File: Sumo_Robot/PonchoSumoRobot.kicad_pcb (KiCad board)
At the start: 2 copper layers, 85.9 x 137.2 mm, 58 parts, among them K1 RELAY_C, K2 RELAY_C, K3 RELAY_C, K4 RELAY_C, P1 CONN_01X02, P11 CONN_01X02, P12 CONN_01X02, P13 CONN_01X02, P14 CONN_01X02, P15 CONN_01X02, P16 CONN_01X02, P17 CONN_01X02, P18 CONN_01X02, P2 CONN_01X04, P3 CONN_02X09, P4 CONN_01X02, P5 CONN_01X02, P6 CONN_01X04, P7 CONN_01X02, P8 CONN_01X02, Q1 2SC1945, Q2 2SC1945, Q3 2SC1945, Q4 2SC1945, Q5 2SC1945, U5 40106

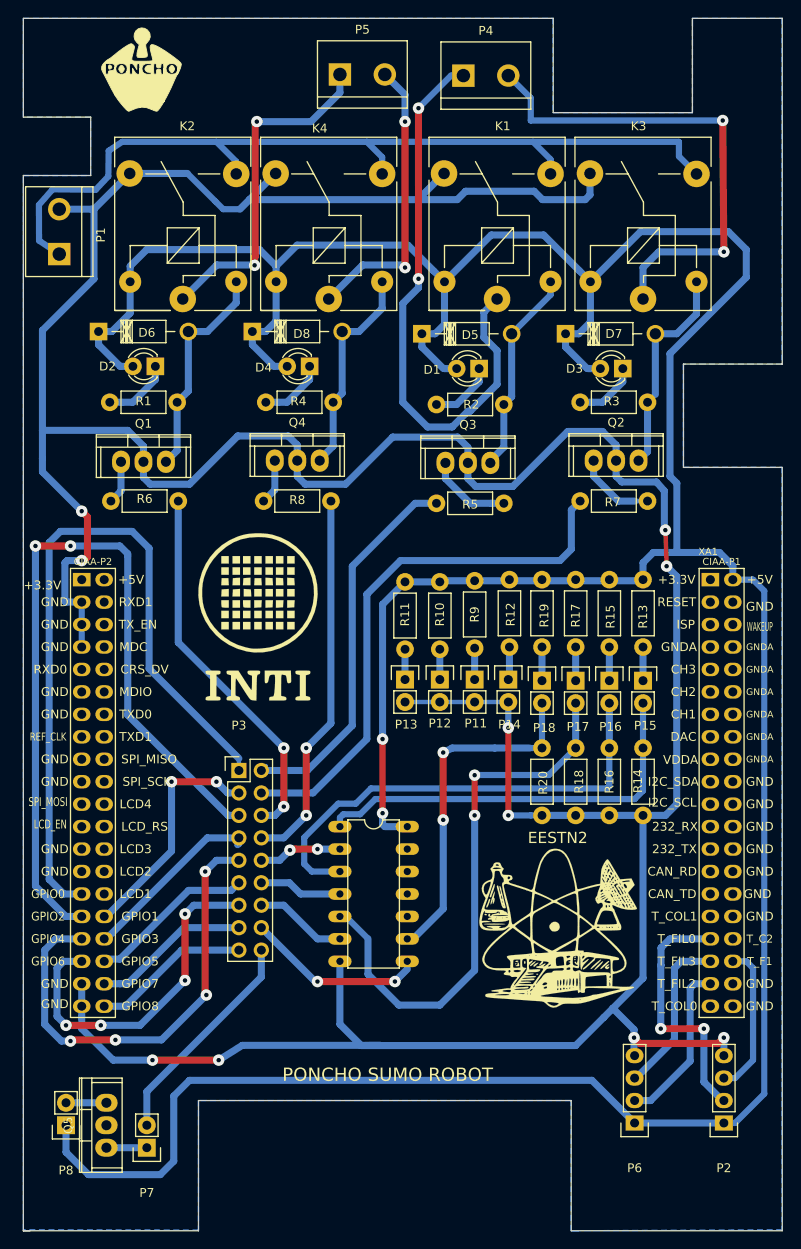
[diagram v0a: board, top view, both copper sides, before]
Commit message: Poncho Sumo Robot: Emprolijo esquemático, serigrafías, vista 3D y textos.
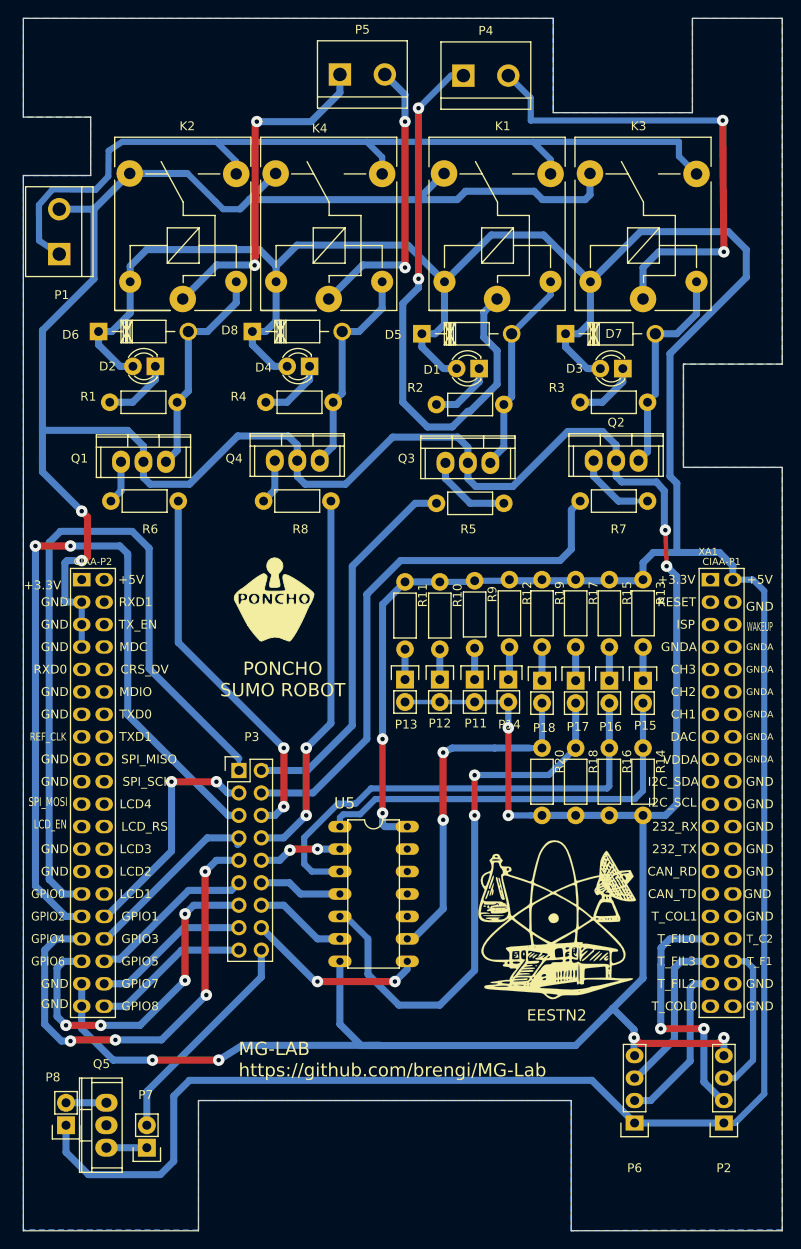
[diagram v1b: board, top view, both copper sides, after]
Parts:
- removed the G*** at (68.2, 96.9)
- R1, R10, R11, R12, R13, R14, R15, R16, R17, R18, R19, R2, R20, R3, R4, R5, R6, R7, R8, R9: footprint sumo_robot:Resistor_Horizontal_RM7mm -> sumo_robot:Resistor_Horizontal_RM7m
- moved G*** 61.8 mm to (70.0, 95.0)
- moved EESTN2 0.96 mm to (102.0, 131.0)
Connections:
- Q5 pad 2: Net-(Q5-Pad2) -> GND
- XA1 pad 1: +3V3 -> (no net)
- XA1 pad 20: Net-(XA1-Pad20) -> (no net)
- XA1 pad 22: Net-(XA1-Pad22) -> (no net)
- XA1 pad 24: Net-(XA1-Pad24) -> (no net)
- XA1 pad 26: Net-(XA1-Pad26) -> (no net)
- XA1 pad 28: Net-(XA1-Pad28) -> (no net)
- XA1 pad 30: Net-(XA1-Pad30) -> (no net)
- XA1 pad 31: Net-(XA1-Pad31) -> (no net)
- XA1 pad 32: Net-(XA1-Pad32) -> (no net)
- XA1 pad 34: Net-(XA1-Pad34) -> (no net)
- XA1 pad 38: Net-(XA1-Pad38) -> (no net)
- XA1 pad 39: Net-(XA1-Pad39) -> (no net)
- XA1 pad 4: Net-(XA1-Pad4) -> (no net)
- XA1 pad 40: Net-(XA1-Pad40) -> (no net)
- XA1 pad 41: Net-(XA1-Pad41) -> (no net)
- XA1 pad 42: +5VP -> (no net)
- XA1 pad 51: Net-(XA1-Pad51) -> (no net)
- XA1 pad 53: Net-(XA1-Pad53) -> (no net)
- XA1 pad 57: Net-(XA1-Pad57) -> (no net)
- XA1 pad 59: Net-(XA1-Pad59) -> (no net)
- XA1 pad 65: Net-(XA1-Pad65) -> (no net)
- XA1 pad 67: Net-(XA1-Pad67) -> (no net)
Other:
- outline, holes or cut-outs redrawn
- board text added: "*Cambiar transistores de los relés a TO92. *Mejorar los puentes."
- board text added: "MG-LAB https://github.com/brengi/MG-Lab"
- board text removed: "*cambiar a TO92. *Falta una conexión. *Referencias debajo de componentes. * Modelos 3D."
